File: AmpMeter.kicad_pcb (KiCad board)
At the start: 2 copper layers, 135.6 x 72.1 mm, 49 parts, among them J1 Vin L1-L3, J2 Serial, J3 ct1, J4 ct2, J5 ct3, J6 ct L1-L3, T1 Transformer_1P_1S, T2 Transformer_1P_1S, T3 Transformer_1P_1S, U1 LTV-817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

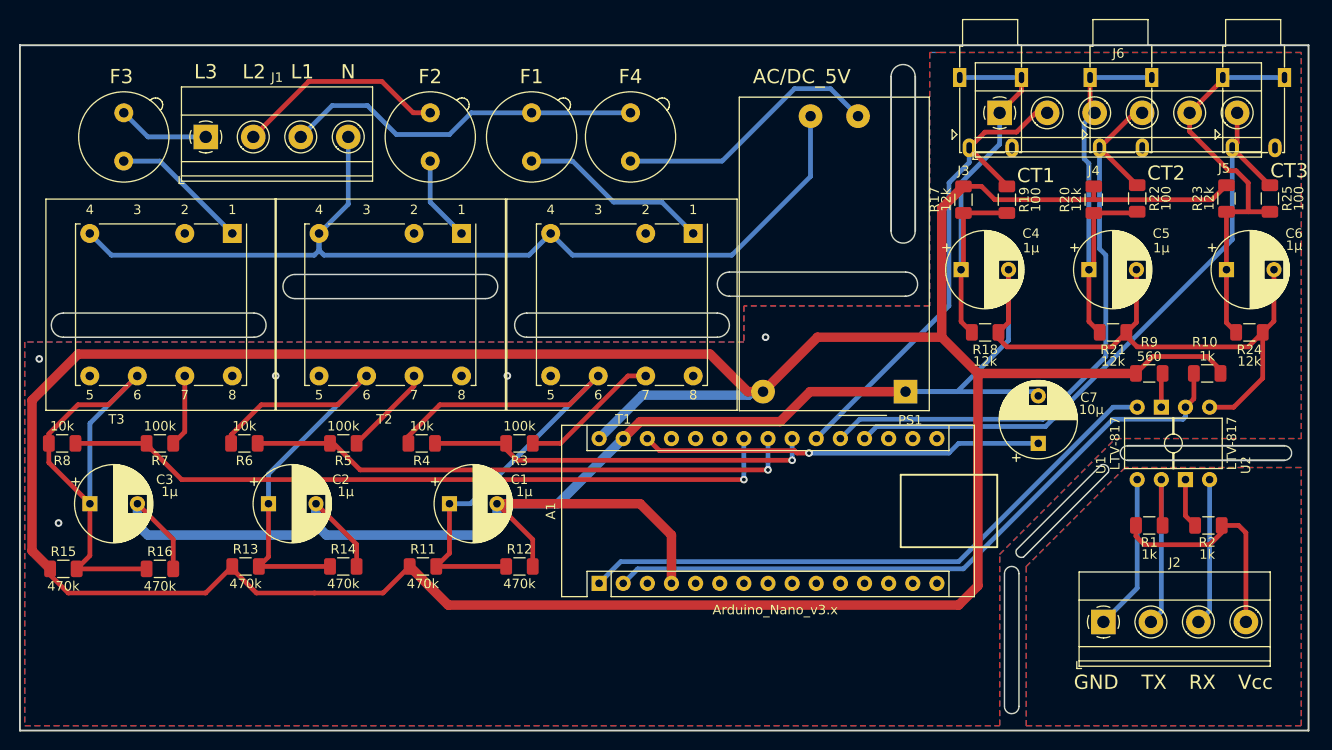
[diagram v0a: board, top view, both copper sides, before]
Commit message: change values on parts
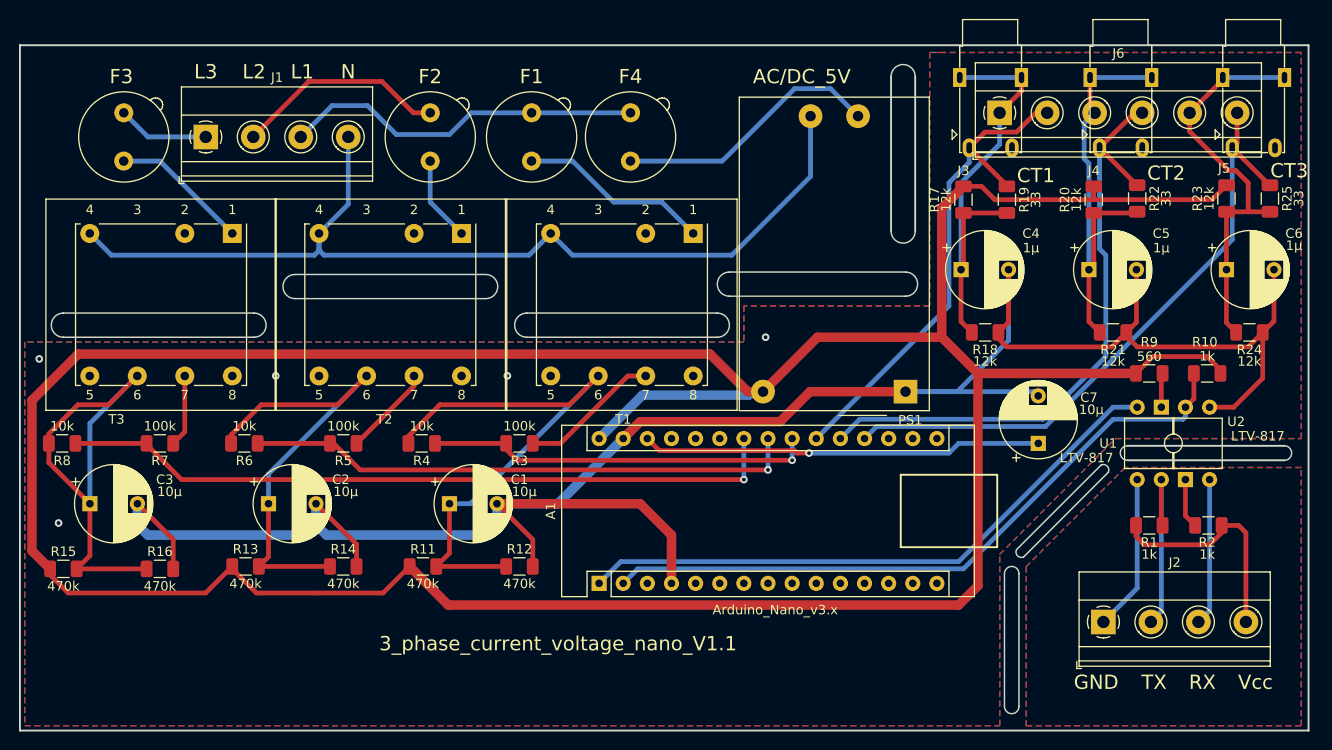
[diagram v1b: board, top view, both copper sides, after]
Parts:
- C1, C2, C3: value 1µ -> 10µ
- R19, R22, R25: value 100 -> 33
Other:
- board text added: "3_phase_current_voltage_nano_V1.1"
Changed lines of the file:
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@@
   (general
     (thickness 1.6)
-    (drawings 58)
+    (drawings 59)
     (tracks 296)
     (zones 0)
@@
     (descr "4-lead though-hole mounted DIP package, row spacing 7.62 mm (300 mils)")
     (tags "THT DIP DIL PDIP 2.54mm 7.62mm 300mil")
-    (fp_text reference U1 (at 1.524 -8.89 90) (layer F.SilkS)
+    (fp_text reference U1 (at 3.81 -8.128 180) (layer F.SilkS)
       (effects (font (size 1 1) (thickness 0.15)))
     )
-    (fp_text value LTV-817 (at 3.81 4.87 90) (layer F.SilkS)
+    (fp_text value LTV-817 (at 4.572 7.62 180) (layer F.SilkS)
       (effects (font (size 1 1) (thickness 0.15)))
     )
@@
     (descr "4-lead though-hole mounted DIP package, row spacing 7.62 mm (300 mils)")
     (tags "THT DIP DIL PDIP 2.54mm 7.62mm 300mil")
-    (fp_text reference U2 (at 6.096 -8.89 270) (layer F.SilkS)
+    (fp_text reference U2 (at 1.524 -7.874) (layer F.SilkS)
       (effects (font (size 1 1) (thickness 0.15)))
     )
-    (fp_text value LTV-817 (at 3.81 4.87 270) (layer F.SilkS)
+    (fp_text value LTV-817 (at 5.334 7.874) (layer F.SilkS)
       (effects (font (size 1 1) (thickness 0.15)))
     )
@@
       (effects (font (size 1 1) (thickness 0.15)))
     )
-    (fp_text value 100 (at 0 -3.048 270) (layer F.SilkS)
+    (fp_text value 33 (at 0 -3.048 270) (layer F.SilkS)
       (effects (font (size 1 1) (thickness 0.15)))
     )
@@
       (effects (font (size 1 1) (thickness 0.15)))
     )
-    (fp_text value 100 (at 0 -3.048 270) (layer F.SilkS)
+    (fp_text value 33 (at 0 -3.048 270) (layer F.SilkS)
       (effects (font (size 1 1) (thickness 0.15)))
     )
@@
       (effects (font (size 1 1) (thickness 0.15)))
     )
-    (fp_text value 100 (at 0 -3.048 270) (layer F.SilkS)
+    (fp_text value 33 (at 0 -3.048 270) (layer F.SilkS)
       (effects (font (size 1 1) (thickness 0.15)))
     )
@@
       (effects (font (size 1 1) (thickness 0.15)))
     )
-    (fp_text value 1µ (at 7.874 -1.27) (layer F.SilkS)
+    (fp_text value 10µ (at 7.874 -1.27) (layer F.SilkS)
       (effects (font (size 1 1) (thickness 0.15)))
     )
@@
       (effects (font (size 1 1) (thickness 0.15)))
     )
-    (fp_text value 1µ (at 8.128 -1.27) (layer F.SilkS)
+    (fp_text value 10µ (at 8.128 -1.27) (layer F.SilkS)
       (effects (font (size 1 1) (thickness 0.15)))
     )
@@
       (effects (font (size 1 1) (thickness 0.15)))
     )
-    (fp_text value 1µ (at 8.382 -1.27) (layer F.SilkS)
+    (fp_text value 10µ (at 8.382 -1.27) (layer F.SilkS)
       (effects (font (size 1 1) (thickness 0.15)))
     )
@@
     )
   )
+  (gr_text 3_phase_current_voltage_nano_V1.1 (at 74.93 73.914) (layer F.SilkS)
+    (effects (font (size 1.5 1.5) (thickness 0.3)))
+  )
   (gr_arc (start 122.682 80.518) (end 121.92 80.518) (angle -180) (layer Edge.Cuts) (width 0.15))
